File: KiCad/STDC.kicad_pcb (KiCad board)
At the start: 4 copper layers, 38 x 48 mm, 127 parts, among them IC1 TPS22916CNYFPR, IC2 TPS22916CNYFPR, IC3 R1200N001A-TR-FE, IC4 MS5849-30BA, IC5 W25Q32JWSNIQ, J1 TC2030, J2 Conn_01x03_BATT, J3 Conn_01x34_NHD_18, Q1 AO3400A, Q2 AO3400A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

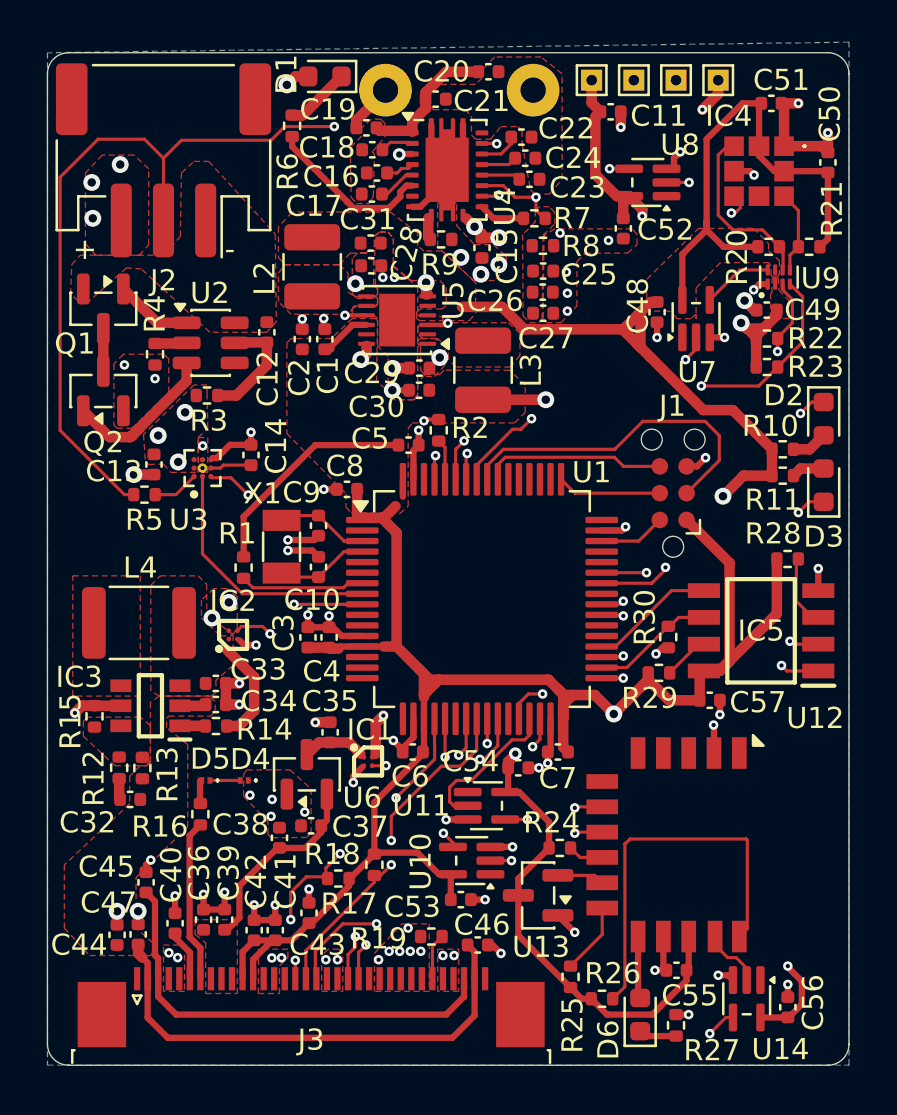
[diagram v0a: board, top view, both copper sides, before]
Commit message: Easier VIA placement
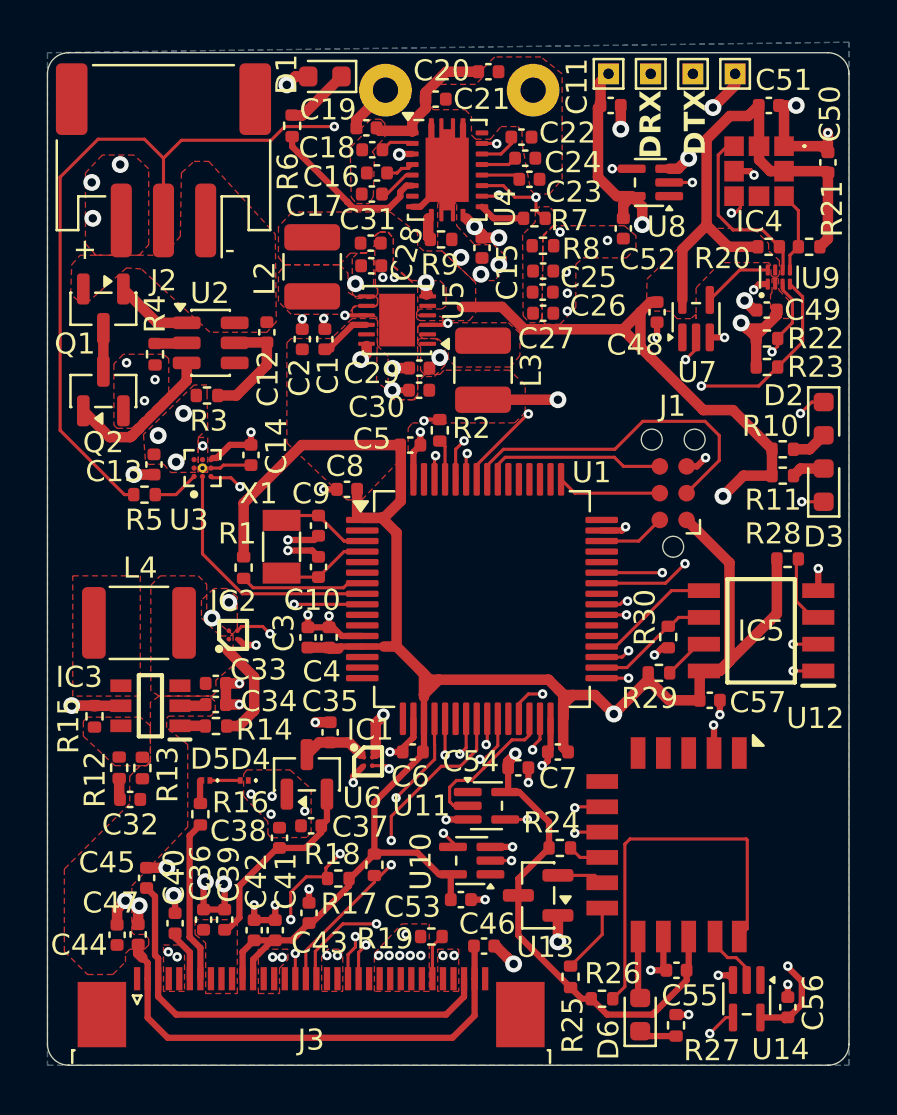
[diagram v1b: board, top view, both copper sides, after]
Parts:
- moved TP1 0.85 mm to (151.6, 101.5)
- moved TP2 0.85 mm to (153.6, 101.5)
- moved TP3 0.85 mm to (155.6, 101.5)
- moved TP4 0.85 mm to (157.6, 101.5)
- moved C46 0.30 mm to (145.7, 142.8)
- moved C11 0.30 mm to (151.7, 103.0)
- moved C45 0.21 mm to (129.7, 139.6)
- moved C51 0.16 mm to (159.2, 103.0)
- moved U8 0.12 mm to (153.6, 106.7)
- moved C5 0.08 mm to (142.2, 119.1)
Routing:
- net GND: track 75.2 -> 79.9 mm, vias 88 -> 89
- net +1V8: track 151.4 -> 154.1 mm
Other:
- board text added: "DRX"
- board text added: "DTX"

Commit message: Use SMT connector for Battery
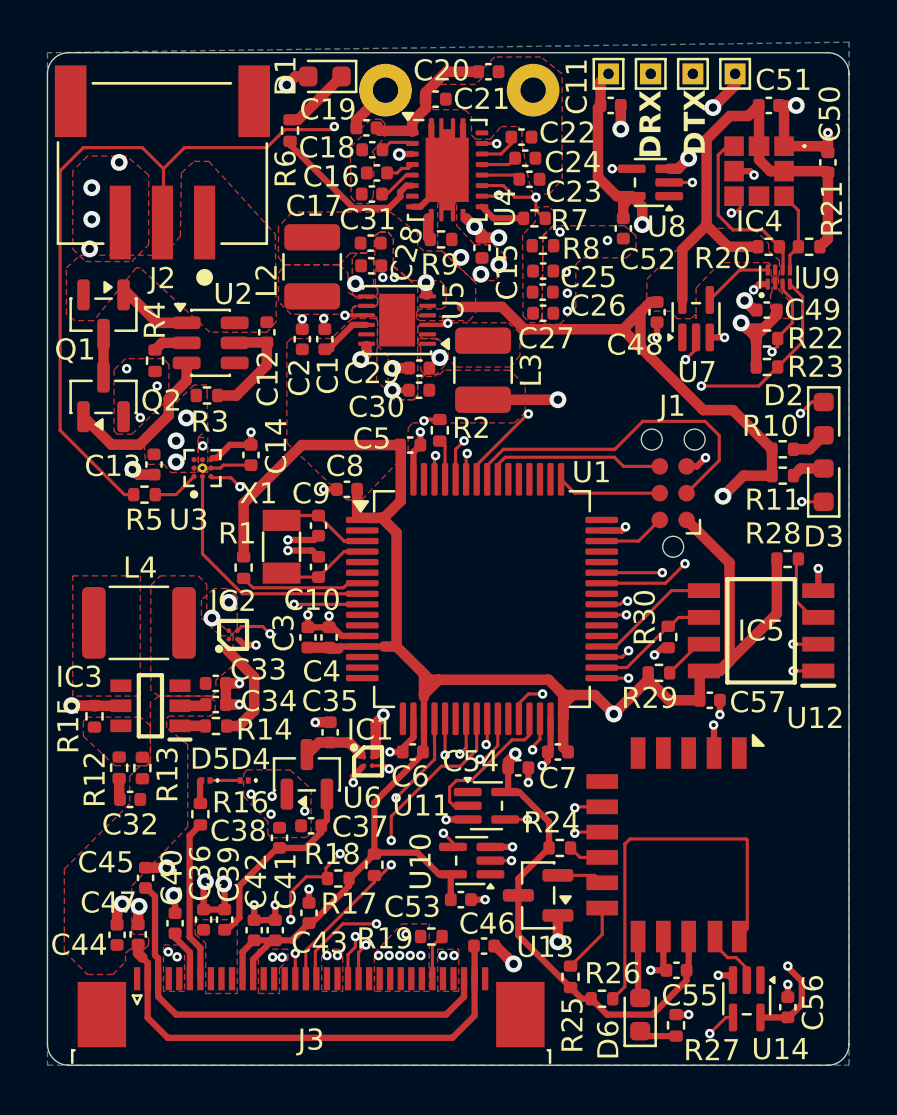
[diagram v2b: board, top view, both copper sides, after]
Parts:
- J2: value Conn_01x03_BATT -> S3B-PH-SM4-TB_LF__SN_; footprint Connector_JST:JST_PH_S3B-PH-SM4-TB_1x03-1MP_P2.00mm_Horizontal -> JST PH S3B Connector:JST_S3B-PH-SM4-TB_LF__SN_
- moved J2 2.95 mm to (130.4, 108.5), turned to 0 degrees
- moved R4 0.31 mm to (130.1, 115.1)
- moved Q2 0.28 mm to (127.7, 116.8)
- moved Q1 0.28 mm to (127.7, 112.9)
- moved R6 0.25 mm to (136.5, 104.2)
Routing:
- net /Power+Battery/OC: track 7.38 -> 8.00 mm
- net /Power+Battery/BATT+: vias 10 -> 11
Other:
- board text removed: "+"
- board text removed: "-"

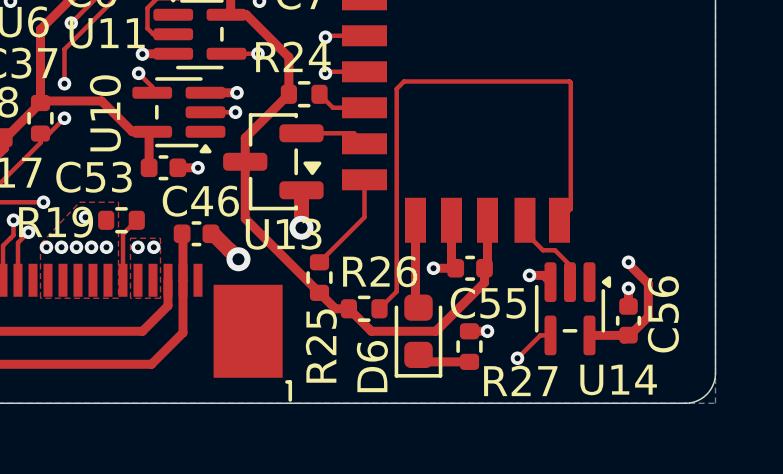
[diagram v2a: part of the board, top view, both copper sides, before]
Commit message: Fix polarity of Bluetooth Status LED
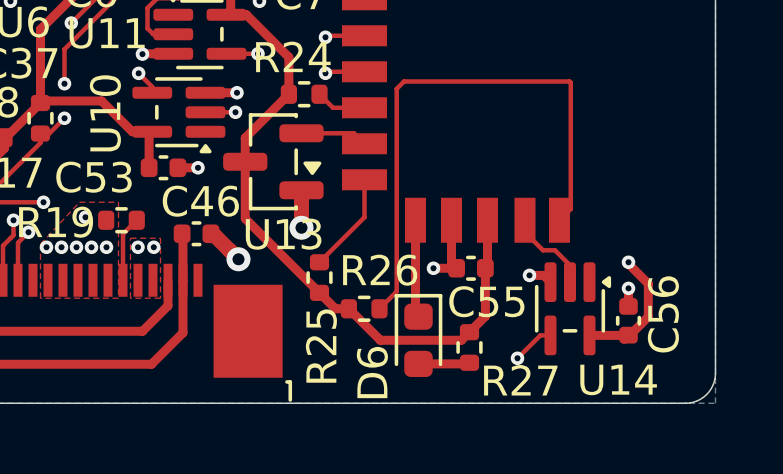
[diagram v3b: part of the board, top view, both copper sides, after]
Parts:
- moved D6 0.30 mm to (153.1, 146.4), turned to -90 degrees
- turned R27 to 90 degrees
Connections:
- D6 pad 1: /Bluetooth Module/Bluetooth_LED_Res -> /Bluetooth Module/Bluetooth_LED
- D6 pad 2: /Bluetooth Module/Bluetooth_LED -> /Bluetooth Module/Bluetooth_LED_Res
- R27 pad 1: GND -> /Bluetooth Module/Bluetooth_LED_Res
- R27 pad 2: /Bluetooth Module/Bluetooth_LED_Res -> +3.3V
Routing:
- net +3.3V: track 102.8 -> 104.2 mm
- net GND: track 79.9 -> 79.5 mm, vias 89 -> 88
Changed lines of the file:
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@@
 	(footprint "Capacitor_SMD:C_0402_1005Metric"
 		(layer "F.Cu")
-		(at 154.82 144 180)
+		(at 154.85 144 180)
 		(descr "Capacitor SMD 0402 (1005 Metric), square (rectangular) end terminal, IPC-7351 nominal, (Body size source: IPC-SM-782 page 76, https://www.pcb-3d.com/wordpress/wp-content/uploads/ipc-sm-782a_amendment_1_and_2.pdf), generated with kicad-footprint-generator")
 		(tags "capacitor")
 		(property "Reference" "C55"
-			(at -0.63 -1.2 180)
+			(at -0.55 -1.15 180)
 			(layer "F.SilkS")
 			(effects
@@
 		(tags "resistor")
 		(property "Reference" "R26"
-			(at 0.51 -1.2 180)
+			(at 0.51 -1.25 180)
 			(layer "F.SilkS")
 			(effects
@@
 	(footprint "Resistor_SMD:R_0402_1005Metric"
 		(layer "F.Cu")
-		(at 154.8 146.61 -90)
+		(at 154.8 146.64 90)
 		(descr "Resistor SMD 0402 (1005 Metric), square (rectangular) end terminal, IPC-7351 nominal, (Body size source: IPC-SM-782 page 72, https://www.pcb-3d.com/wordpress/wp-content/uploads/ipc-sm-782a_amendment_1_and_2.pdf), generated with kicad-footprint-generator")
 		(tags "resistor")
 		(property "Reference" "R27"
-			(at 1.19 -1.7 0)
+			(at -1.14 1.7 0)
 			(layer "F.SilkS")
 			(effects
@@
 		(attr smd)
 		(fp_line
-			(start -0.153641 0.38)
-			(end 0.153641 0.38)
+			(start -0.153641 -0.38)
+			(end 0.153641 -0.38)
 			(stroke
 				(width 0.12)
@@
 		)
 		(fp_line
-			(start -0.153641 -0.38)
-			(end 0.153641 -0.38)
+			(start -0.153641 0.38)
+			(end 0.153641 0.38)
 			(stroke
 				(width 0.12)
@@
 		)
 		(pad "1" smd roundrect
-			(at -0.51 0 270)
+			(at -0.51 0 90)
 			(size 0.54 0.64)
 			(layers "F.Cu" "F.Mask" "F.Paste")
 			(roundrect_rratio 0.25)
-			(net 2 "GND")
+			(net 25 "/Bluetooth Module/Bluetooth_LED_Res")
 			(pintype "passive")
 		)
 		(pad "2" smd roundrect
-			(at 0.51 0 270)
+			(at 0.51 0 90)
 			(size 0.54 0.64)
 			(layers "F.Cu" "F.Mask" "F.Paste")
 			(roundrect_rratio 0.25)
-			(net 25 "/Bluetooth Module/Bluetooth_LED_Res")
+			(net 14 "+3.3V")
 			(pintype "passive")
 		)
@@
 	(footprint "LED_SMD:LED_0603_1608Metric"
 		(layer "F.Cu")
-		(at 153.1 146.1 90)
+		(at 153.1 146.4 -90)
 		(descr "LED SMD 0603 (1608 Metric), square (rectangular) end terminal, IPC-7351 nominal, (Body size source: http://www.tortai-tech.com/upload/download/2011102023233369053.pdf), generated with kicad-footprint-generator")
 		(tags "LED")
 		(property "Reference" "D6"
-			(at -1.2 -1.5 270)
+			(at 1.1 1.5 270)
 			(layer "F.SilkS")
 			(effects
@@
 		)
 		(property "Sim.Pins" "1=K 2=A"
-			(at 0 0 90)
+			(at 0 0 270)
 			(unlocked yes)
 			(layer "F.Fab")
@@
 		(attr smd)
 		(fp_line
-			(start 0.8 -0.735)
-			(end -1.485 -0.735)
+			(start -1.485 0.735)
+			(end 0.8 0.735)
 			(stroke
 				(width 0.12)
@@
 		)
 		(fp_line
-			(start -1.485 0.735)
-			(end 0.8 0.735)
+			(start 0.8 -0.735)
+			(end -1.485 -0.735)
 			(stroke
 				(width 0.12)
@@
 		)
 		(fp_line
-			(start 0.8 -0.4)
-			(end -0.5 -0.4)
+			(start -0.8 0.4)
+			(end 0.8 0.4)
 			(stroke
 				(width 0.1)
@@
 		)
 		(fp_line
-			(start -0.5 -0.4)
-			(end -0.8 -0.1)
+			(start 0.8 0.4)
+			(end 0.8 -0.4)
 			(stroke
 				(width 0.1)
@@
 		)
 		(fp_line
-			(start 0.8 0.4)
-			(end 0.8 -0.4)
+			(start -0.5 -0.4)
+			(end -0.8 -0.1)
 			(stroke
 				(width 0.1)
@@
 		)
 		(fp_line
-			(start -0.8 0.4)
-			(end 0.8 0.4)
+			(start 0.8 -0.4)
+			(end -0.5 -0.4)
 			(stroke
 				(width 0.1)
@@
 		)
 		(pad "1" smd roundrect
-			(at -0.7875 0 90)
+			(at -0.7875 0 270)
 			(size 0.875 0.95)
 			(layers "F.Cu" "F.Mask" "F.Paste")
 			(roundrect_rratio 0.25)
-			(net 25 "/Bluetooth Module/Bluetooth_LED_Res")
+			(net 24 "/Bluetooth Module/Bluetooth_LED")
 			(pinfunction "K")
 			(pintype "passive")
 		)
 		(pad "2" smd roundrect
-			(at 0.7875 0 90)
+			(at 0.7875 0 270)
 			(size 0.875 0.95)
 			(layers "F.Cu" "F.Mask" "F.Paste")
 			(roundrect_rratio 0.25)
-			(net 24 "/Bluetooth Module/Bluetooth_LED")
+			(net 25 "/Bluetooth Module/Bluetooth_LED_Res")
 			(pinfunction "A")
 			(pintype "passive")
@@
 	)
 	(segment
+		(start 154.2 143.83)
+		(end 154.37 144)
+		(width 0.3)
+		(layer "F.Cu")
+		(net 2)
+	)
+	(segment
 		(start 152.234524 123.15)
 		(end 151.275 123.15)
@@
 	)
 	(segment
-		(start 154.8 146.1)
-		(end 155.4 146.1)
-		(width 0.3)
-		(layer "F.Cu")
-		(net 2)
-	)
-	(segment
 		(start 161.71 104.93)
 		(end 162 105.22)
@@
 	)
 	(segment
-		(start 154.2 142.4)
-		(end 154.2 143.86)
-		(width 0.3)
-		(layer "F.Cu")
-		(net 2)
-	)
-	(segment
 		(start 137.35 127.74)
 		(end 137.35 127.15)
@@
 		(net 2)
 	)
+	(segment
+		(start 154.2 142.4)
+		(end 154.2 143.83)
+		(width 0.3)
+		(layer "F.Cu")
+		(net 2)
+	)
 	(via
 		(at 137.7 132.25)
@@
 	)
 	(via
-		(at 155.4 146.1)
-		(size 0.45)
-		(drill 0.2)
-		(layers "F.Cu" "B.Cu")
-		(net 2)
-	)
-	(via
 		(at 142.85 117.95)
 		(size 0.45)
@@
 	)
 	(segment
+		(start 150.78 145.35)
+		(end 151.83 146.4)
+		(width 0.3)
+		(layer "F.Cu")
+		(net 14)
+	)
+	(segment
 		(start 147.119087 133.794087)
 		(end 147.119087 133.830913)
@@
 	(segment
 		(start 155.4 142.4)
-		(end 155.4 143.9)
+		(end 155.4 143.55)
 		(width 0.3)
 		(layer "F.Cu")
@@
 	)
 	(segment
+		(start 154.53 146.4)
+		(end 154.8 146.13)
+		(width 0.3)
+		(layer "F.Cu")
+		(net 14)
+	)
+	(segment
 		(start 159.35 120.55)
 		(end 159.35 119.3)
@@
 	)
 	(segment
+		(start 155.4 143.55)
+		(end 155.4 143.93)
+		(width 0.3)
+		(layer "F.Cu")
+		(net 14)
+	)
+	(segment
 		(start 155.1 112.22)
 		(end 155.1 109.825)
@@
 	)
 	(segment
-		(start 153.679 146.1)
-		(end 155.3 144.479)
-		(width 0.3)
-		(layer "F.Cu")
-		(net 14)
-	)
-	(segment
 		(start 158.735 104.93)
 		(end 158.735 105.577)
@@
 	)
 	(segment
+		(start 155.33 145.6)
+		(end 155.33 144)
+		(width 0.3)
+		(layer "F.Cu")
+		(net 14)
+	)
+	(segment
+		(start 155.4 143.55)
+		(end 155.4 143.9)
+		(width 0.3)
+		(layer "F.Cu")
+		(net 14)
+	)
+	(segment
 		(start 159.273 106.115)
 		(end 159.92 106.115)
@@
 	)
 	(segment
-		(start 151.53 146.1)
-		(end 153.679 146.1)
-		(width 0.3)
-		(layer "F.Cu")
-		(net 14)
-	)
-	(segment
 		(start 152.261058 113.611)
 		(end 152.299001 113.611)
@@
 	)
 	(segment
-		(start 159.35 120.55)
-		(end 158 120.55)
-		(width 0.5)
+		(start 154.8 146.13)
+		(end 155.33 145.6)
+		(width 0.3)
 		(layer "F.Cu")
 		(net 14)
 	)
 	(segment
-		(start 155.3 144.479)
-		(end 155.3 144)
-		(width 0.3)
+		(start 159.35 120.55)
+		(end 158 120.55)
+		(width 0.5)
 		(layer "F.Cu")
 		(net 14)
@@
 	)
 	(segment
+		(start 155.4 143.93)
+		(end 155.33 144)
+		(width 0.3)
+		(layer "F.Cu")
+		(net 14)
+	)
+	(segment
 		(start 156.25 104.6)
 		(end 156.25 108.675)
@@
 	)
 	(segment
-		(start 147.362499 135.55)
-		(end 148.78 136.967501)
+		(start 151.83 146.4)
+		(end 154.53 146.4)
 		(width 0.3)
 		(layer "F.Cu")
@@
 	)
 	(segment
-		(start 150.78 145.35)
-		(end 151.53 146.1)
+		(start 147.362499 135.55)
+		(end 148.78 136.967501)
 		(width 0.3)
 		(layer "F.Cu")
@@
 	(segment
 		(start 153 142.4)
-		(end 153 145.2125)
+		(end 153 145.4)
 		(width 0.3)
 		(layer "F.Cu")
@@
 	)
 	(segment
-		(start 153 145.2125)
-		(end 153.1 145.3125)
+		(start 153.1 145.5)
+		(end 153 145.4)
 		(width 0.3)
 		(layer "F.Cu")
@@
 	)
 	(segment
-		(start 153.3325 147.12)
-		(end 153.1 146.8875)
+		(start 153.1 147.1875)
+		(end 154.7625 147.1875)
 		(width 0.3)
 		(layer "F.Cu")
@@
 	)
 	(segment
-		(start 154.8 147.12)
-		(end 153.3325 147.12)
+		(start 154.7625 147.1875)
+		(end 154.8 147.15)
 		(width 0.3)
 		(layer "F.Cu")

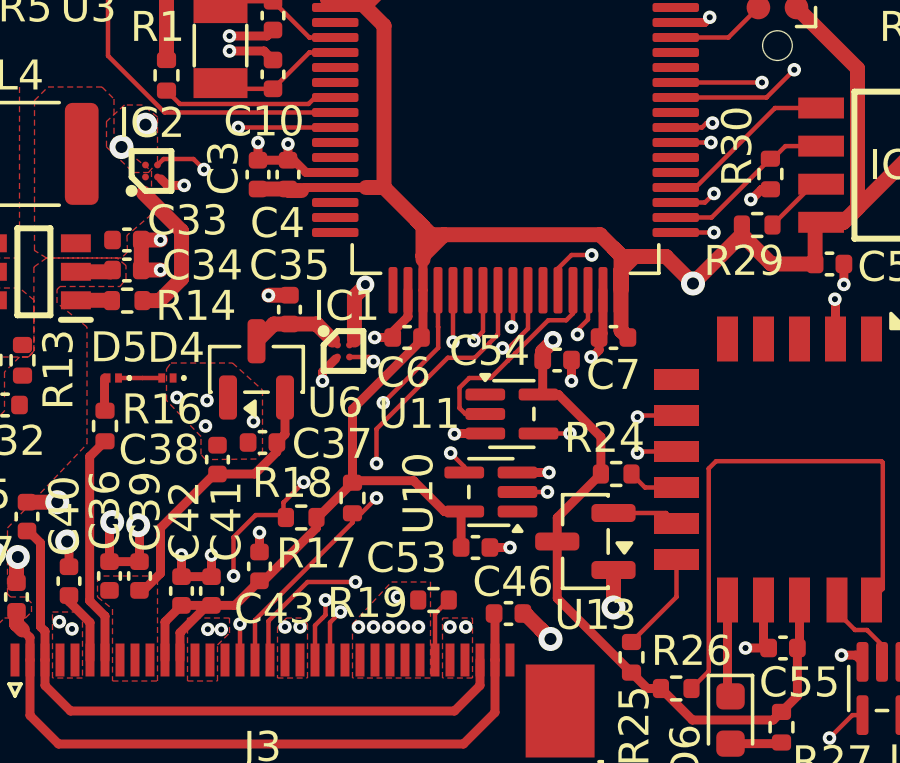
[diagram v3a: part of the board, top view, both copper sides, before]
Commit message: Reduce Cuts in reference plane
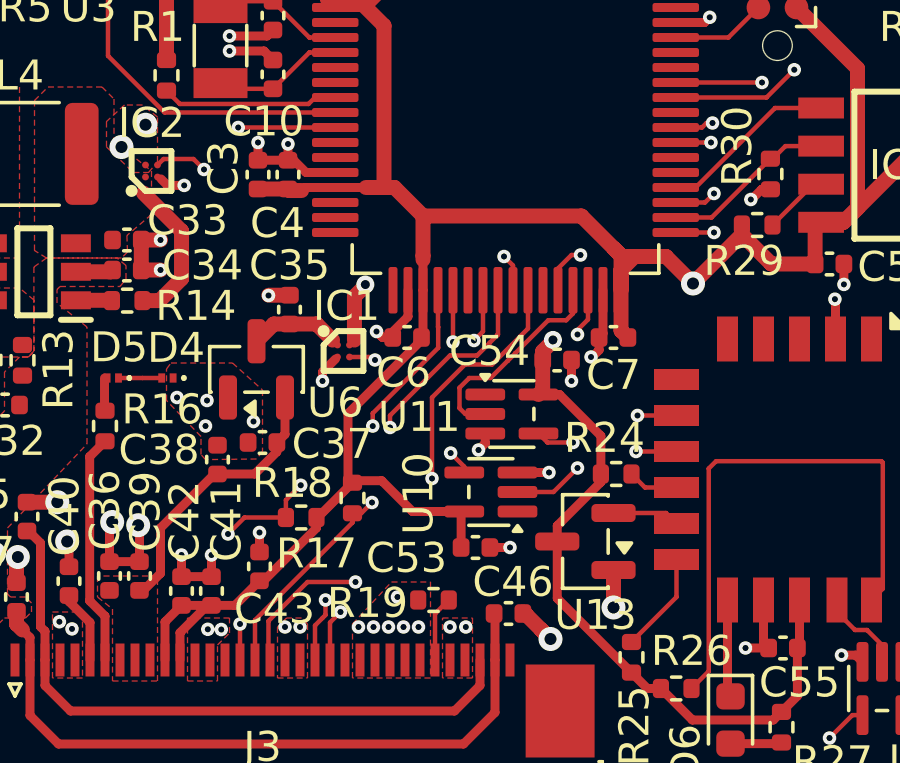
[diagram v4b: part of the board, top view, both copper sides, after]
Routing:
- net DISPLAY_EN: track 19.5 -> 21.2 mm
- net +3.3V: track 104.2 -> 102.5 mm
- net /BLE_TX_IND: track 26.3 -> 25.0 mm
- net +1V8: track 154.1 -> 153.3 mm
- net //Display_SPI_CS: track 15.9 -> 16.6 mm
